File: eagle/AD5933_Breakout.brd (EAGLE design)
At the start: 38.1 x 25.4 mm, 6 parts, among them U1 AD5933

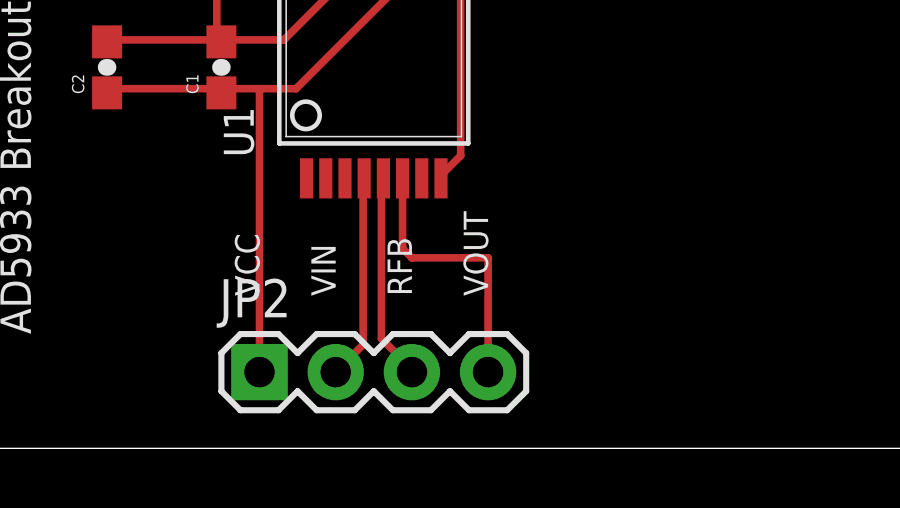
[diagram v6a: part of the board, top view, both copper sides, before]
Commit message: fixed rules and cleared clearance errors
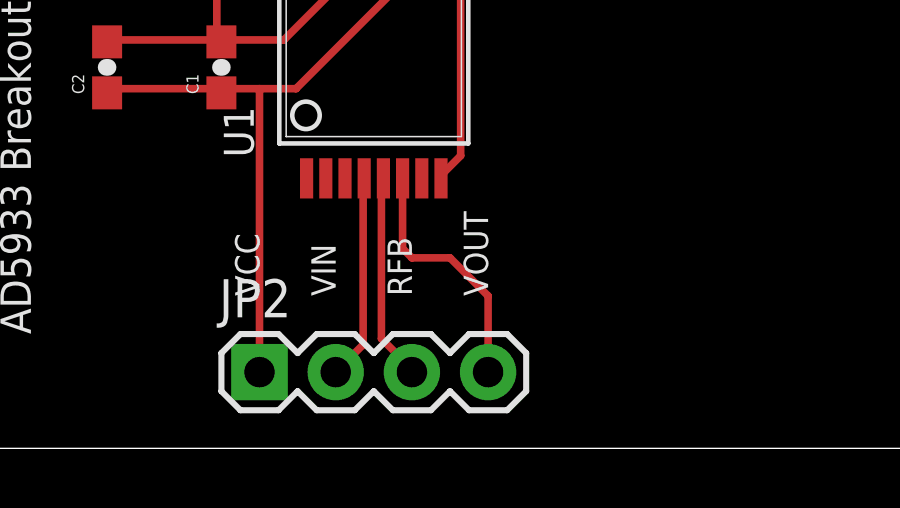
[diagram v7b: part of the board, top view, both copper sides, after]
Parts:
- removed FRAME1: FRAME-LETTER, SparkFun-Aesthetics:CREATIVE_COMMONS
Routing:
- net VOUT: track 9.13 -> 8.38 mm
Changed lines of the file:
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@@
 <?xml version="1.0" encoding="utf-8"?>
 <!DOCTYPE eagle SYSTEM "eagle.dtd">
-<eagle version="6.5.0">
+<eagle version="6.4">
 <drawing>
 <settings>
@@
 <layers>
 <layer number="1" name="Top" color="4" fill="1" visible="yes" active="yes"/>
+<layer number="2" name="Route2" color="1" fill="3" visible="no" active="yes"/>
+<layer number="3" name="Route3" color="4" fill="3" visible="no" active="yes"/>
+<layer number="4" name="Route4" color="1" fill="4" visible="no" active="yes"/>
+<layer number="5" name="Route5" color="4" fill="4" visible="no" active="yes"/>
+<layer number="6" name="Route6" color="1" fill="8" visible="no" active="yes"/>
+<layer number="7" name="Route7" color="4" fill="8" visible="no" active="yes"/>
+<layer number="8" name="Route8" color="1" fill="2" visible="no" active="yes"/>
+<layer number="9" name="Route9" color="4" fill="2" visible="no" active="yes"/>
+<layer number="10" name="Route10" color="1" fill="7" visible="no" active="yes"/>
+<layer number="11" name="Route11" color="4" fill="7" visible="no" active="yes"/>
+<layer number="12" name="Route12" color="1" fill="5" visible="no" active="yes"/>
+<layer number="13" name="Route13" color="4" fill="5" visible="no" active="yes"/>
+<layer number="14" name="Route14" color="1" fill="6" visible="no" active="yes"/>
+<layer number="15" name="Route15" color="4" fill="6" visible="no" active="yes"/>
 <layer number="16" name="Bottom" color="1" fill="1" visible="yes" active="yes"/>
 <layer number="17" name="Pads" color="2" fill="1" visible="yes" active="yes"/>
@@
 </class>
 </classes>
-<designrules name="default">
+<designrules name="default *">
 <description language="de">&lt;b&gt;EAGLE Design Rules&lt;/b&gt;
 &lt;p&gt;
@@
 <param name="mtCopper" value="0.035mm 0.035mm 0.035mm 0.035mm 0.035mm 0.035mm 0.035mm 0.035mm 0.035mm 0.035mm 0.035mm 0.035mm 0.035mm 0.035mm 0.035mm 0.035mm"/>
 <param name="mtIsolate" value="1.5mm 0.15mm 0.2mm 0.15mm 0.2mm 0.15mm 0.2mm 0.15mm 0.2mm 0.15mm 0.2mm 0.15mm 0.2mm 0.15mm 0.2mm"/>
-<param name="mdWireWire" value="8mil"/>
-<param name="mdWirePad" value="8mil"/>
-<param name="mdWireVia" value="8mil"/>
-<param name="mdPadPad" value="8mil"/>
-<param name="mdPadVia" value="8mil"/>
-<param name="mdViaVia" value="8mil"/>
-<param name="mdSmdPad" value="8mil"/>
-<param name="mdSmdVia" value="8mil"/>
-<param name="mdSmdSmd" value="8mil"/>
+<param name="mdWireWire" value="6mil"/>
+<param name="mdWirePad" value="6mil"/>
+<param name="mdWireVia" value="6mil"/>
+<param name="mdPadPad" value="6mil"/>
+<param name="mdPadVia" value="6mil"/>
+<param name="mdViaVia" value="6mil"/>
+<param name="mdSmdPad" value="6mil"/>
+<param name="mdSmdVia" value="6mil"/>
+<param name="mdSmdSmd" value="6mil"/>
 <param name="mdViaViaSameLayer" value="8mil"/>
 <param name="mnLayersViaInSmd" value="2"/>
@@
 <elements>
 <element name="U1" library="kblom" package="SSOP16" value="AD5933" x="19.05" y="12.7"/>
-<element name="FRAME1" library="SparkFun-Aesthetics" package="CREATIVE_COMMONS" value="FRAME-LETTER" x="-10.16" y="-13.97"/>
 <element name="C1" library="SparkFun-Capacitors" package="0603-CAP" value="0.1uF" x="13.97" y="12.7" rot="R90">
 <attribute name="PROD_ID" value="CAP-08390" x="35.56" y="50.8" size="1.778" layer="27" rot="R90" display="off"/>
@@
 <wire x1="20.01" y1="9" x2="20.01" y2="6.66" width="0.254" layer="1"/>
 <wire x1="20.01" y1="6.66" x2="20.32" y2="6.35" width="0.254" layer="1"/>
-<wire x1="20.32" y1="6.35" x2="22.86" y2="6.35" width="0.254" layer="1"/>
-<wire x1="22.86" y1="6.35" x2="22.86" y2="2.54" width="0.254" layer="1"/>
+<wire x1="20.32" y1="6.35" x2="21.59" y2="6.35" width="0.254" layer="1"/>
+<wire x1="21.59" y1="6.35" x2="22.86" y2="5.08" width="0.254" layer="1"/>
+<wire x1="22.86" y1="5.08" x2="22.86" y2="2.54" width="0.254" layer="1"/>
 </signal>
 <signal name="GND">

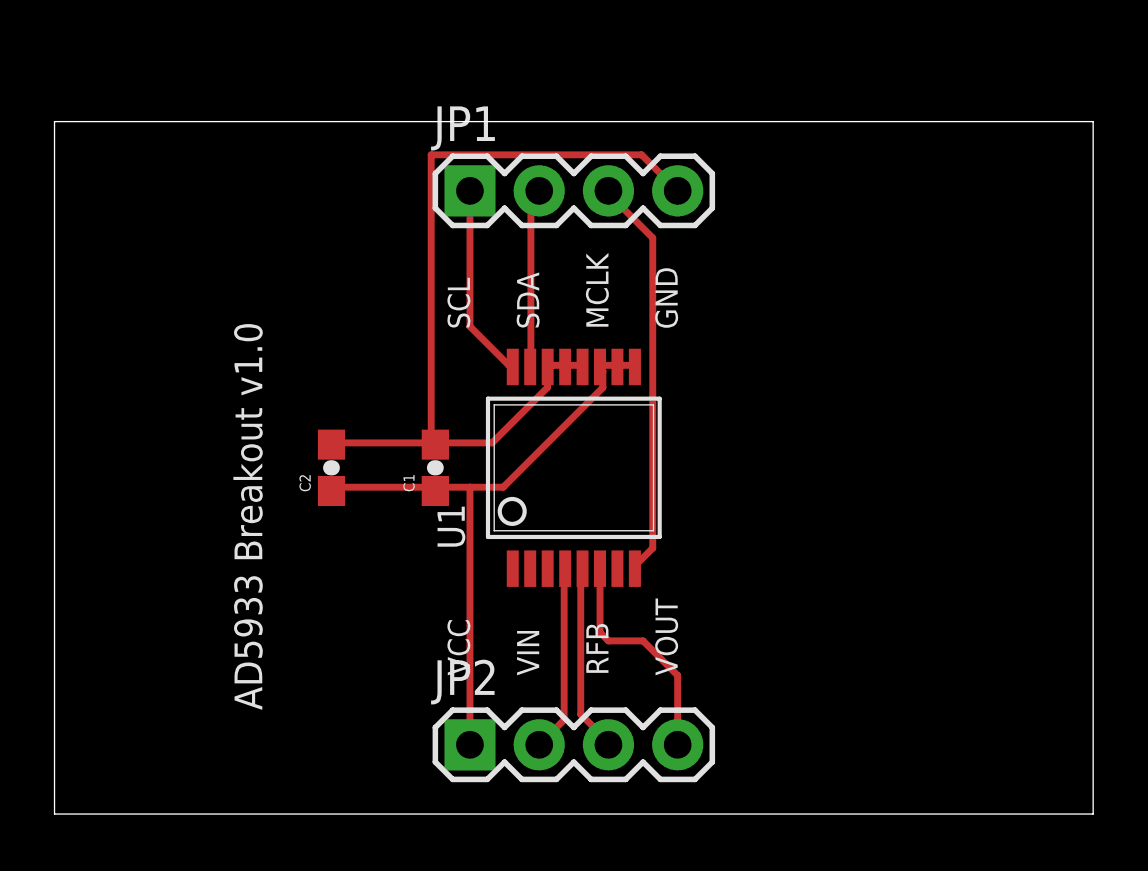
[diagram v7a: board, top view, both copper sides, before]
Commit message: augmented size to fit on breadboard
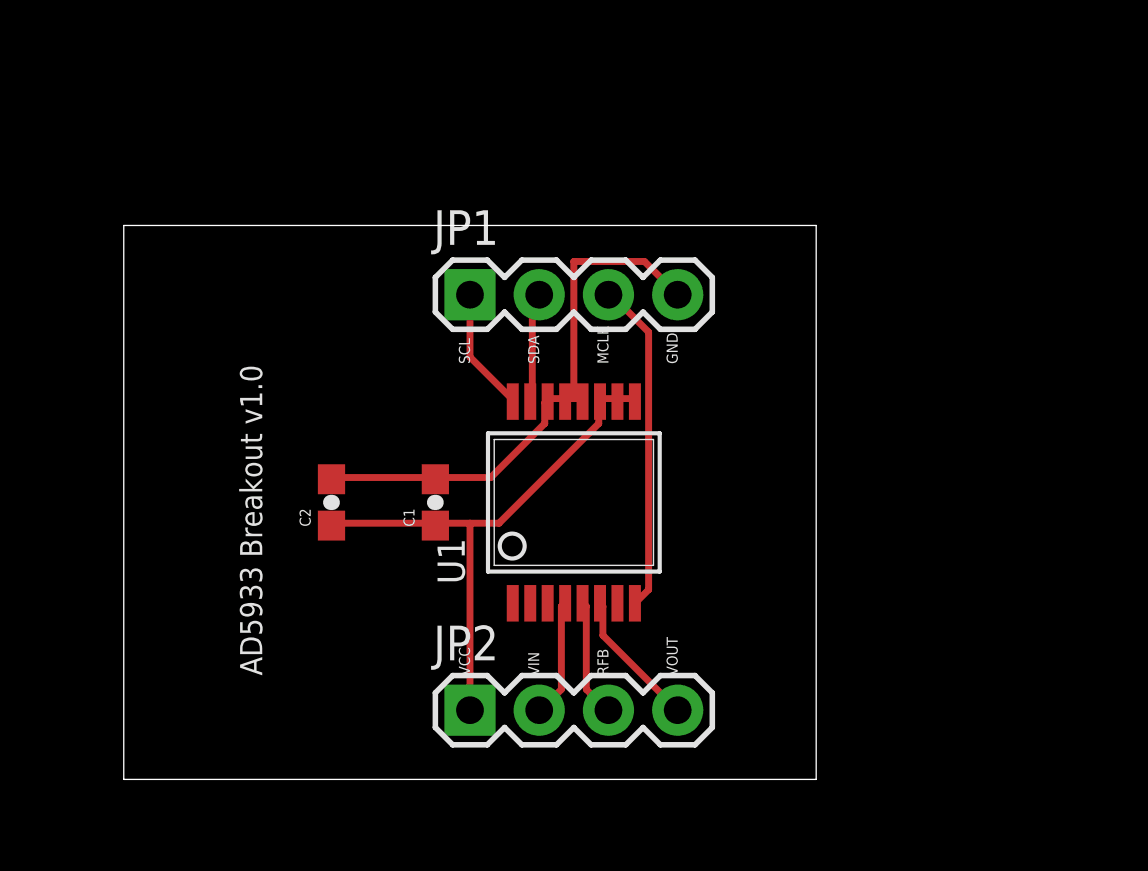
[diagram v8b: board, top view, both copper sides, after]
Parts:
- moved JP1 3.81 mm to (15.2, 19.1)
- moved JP2 1.27 mm to (15.2, 3.81)
- moved C1 1.27 mm to (14.0, 11.4)
- moved C2 1.27 mm to (10.2, 11.4)
- moved U1 1.27 mm to (19.1, 11.4)
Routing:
- net GND: track 31.1 -> 20.5 mm
- net VOUT: track 8.38 -> 5.10 mm
- net VCC: track 23.3 -> 20.6 mm
- net MCLK: track 14.8 -> 12.2 mm
- net SCL: track 7.15 -> 4.56 mm
- net VIN: track 6.91 -> 4.35 mm
- net RFB: track 6.85 -> 4.35 mm
- net SDA: track 6.59 -> 4.11 mm
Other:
- board size 38.1 x 25.4 mm -> 25.4 x 20.3 mm
